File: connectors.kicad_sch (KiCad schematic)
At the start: 4 parts

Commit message: Changes and add component values
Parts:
- gave numbers to parts that had none: 4
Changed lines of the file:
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@@
   (symbol (lib_id "Connector:Conn_01x04_Male") (at 106.68 83.82 0) (unit 1)
     (in_bom yes) (on_board yes)
-    (property "Reference" "J?" (id 0) (at 107.315 76.2 0))
+    (property "Reference" "J1" (id 0) (at 107.315 76.2 0))
     (property "Value" "Conn_01x04_Male" (id 1) (at 107.315 78.74 0))
     (property "Footprint" "" (id 2) (at 106.68 83.82 0)
@@
   (symbol (lib_id "Connector:Conn_01x09_Male") (at 160.02 91.44 0) (unit 1)
     (in_bom yes) (on_board yes)
-    (property "Reference" "J?" (id 0) (at 160.655 76.2 0))
+    (property "Reference" "J3" (id 0) (at 160.655 76.2 0))
     (property "Value" "Conn_01x09_Male" (id 1) (at 160.655 78.74 0))
     (property "Footprint" "" (id 2) (at 160.02 91.44 0)
@@
   (symbol (lib_id "Connector:Conn_01x04_Male") (at 129.54 83.82 0) (unit 1)
     (in_bom yes) (on_board yes)
-    (property "Reference" "J?" (id 0) (at 130.175 76.2 0))
+    (property "Reference" "J2" (id 0) (at 130.175 76.2 0))
     (property "Value" "Conn_01x04_Male" (id 1) (at 130.175 78.74 0))
     (property "Footprint" "" (id 2) (at 129.54 83.82 0)
@@
   (symbol (lib_id "Connector_Generic:Conn_02x03_Odd_Even") (at 187.96 83.82 0) (unit 1)
     (in_bom yes) (on_board yes)
-    (property "Reference" "J?" (id 0) (at 189.23 74.93 0))
+    (property "Reference" "J4" (id 0) (at 189.23 74.93 0))
     (property "Value" "Conn_02x03_Odd_Even" (id 1) (at 189.23 77.47 0))
     (property "Footprint" "" (id 2) (at 187.96 83.82 0)

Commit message: Completed symbol-footprint associations.
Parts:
- J1, J2: footprint (none) -> Connector_PinHeader_2.54mm:PinHeader_1x04_P2.54mm_Vertical
- J3: footprint (none) -> Connector_PinHeader_2.54mm:PinHeader_1x09_P2.54mm_Vertical
- J4: footprint (none) -> Connector_PinHeader_2.54mm:PinHeader_2x03_P2.54mm_Vertical
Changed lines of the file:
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@@
     (property "Reference" "J1" (id 0) (at 107.315 76.2 0))
     (property "Value" "Conn_01x04_Male" (id 1) (at 107.315 78.74 0))
-    (property "Footprint" "" (id 2) (at 106.68 83.82 0)
+    (property "Footprint" "Connector_PinHeader_2.54mm:PinHeader_1x04_P2.54mm_Vertical" (id 2) (at 106.68 83.82 0)
       (effects (font (size 1.27 1.27)) hide)
     )
@@
     (property "Reference" "J3" (id 0) (at 160.655 76.2 0))
     (property "Value" "Conn_01x09_Male" (id 1) (at 160.655 78.74 0))
-    (property "Footprint" "" (id 2) (at 160.02 91.44 0)
+    (property "Footprint" "Connector_PinHeader_2.54mm:PinHeader_1x09_P2.54mm_Vertical" (id 2) (at 160.02 91.44 0)
       (effects (font (size 1.27 1.27)) hide)
     )
@@
     (property "Reference" "J2" (id 0) (at 130.175 76.2 0))
     (property "Value" "Conn_01x04_Male" (id 1) (at 130.175 78.74 0))
-    (property "Footprint" "" (id 2) (at 129.54 83.82 0)
+    (property "Footprint" "Connector_PinHeader_2.54mm:PinHeader_1x04_P2.54mm_Vertical" (id 2) (at 129.54 83.82 0)
       (effects (font (size 1.27 1.27)) hide)
     )
@@
     (property "Reference" "J4" (id 0) (at 189.23 74.93 0))
     (property "Value" "Conn_02x03_Odd_Even" (id 1) (at 189.23 77.47 0))
-    (property "Footprint" "" (id 2) (at 187.96 83.82 0)
+    (property "Footprint" "Connector_PinHeader_2.54mm:PinHeader_2x03_P2.54mm_Vertical" (id 2) (at 187.96 83.82 0)
       (effects (font (size 1.27 1.27)) hide)
     )

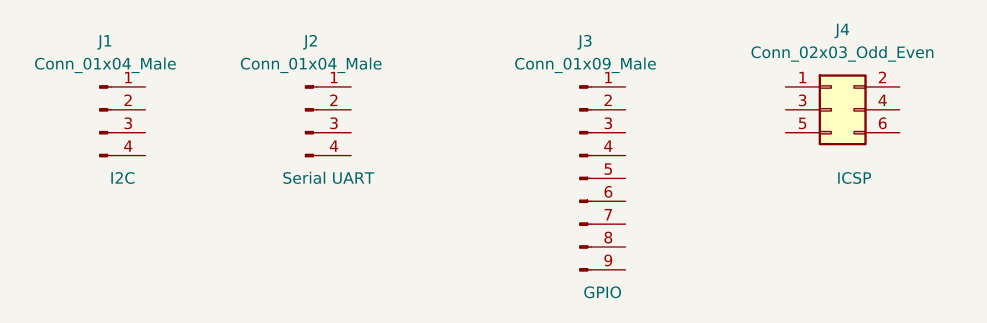
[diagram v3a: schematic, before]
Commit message: Completed wiring
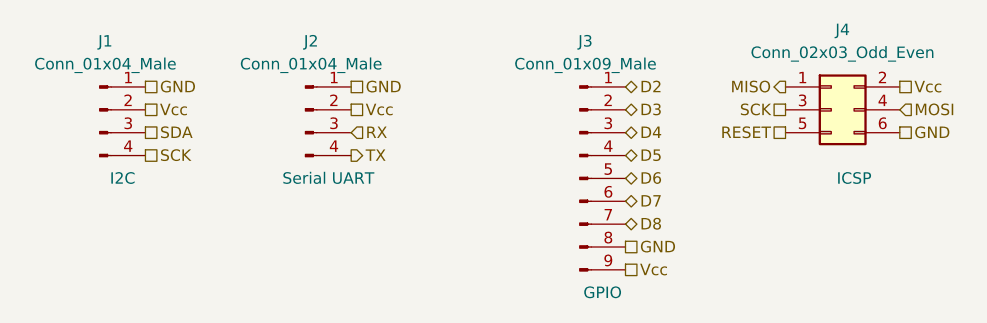
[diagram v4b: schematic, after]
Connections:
- net GND: now reaches J1.1 (Pin_1)
- net GND: now also J2.1 (Pin_1), J3.8 (Pin_8), J4.6 (Pin_6)
- net Vcc: now reaches J1.2 (Pin_2)
- net Vcc: now also J2.2 (Pin_2), J3.9 (Pin_9), J4.2 (Pin_2)
- net SDA: now reaches J1.3 (Pin_3)
- net SCK: now reaches J1.4 (Pin_4)
- net SCK: now also J4.3 (Pin_3)
- net D2: now reaches J3.1 (Pin_1)
- net D3: now reaches J3.2 (Pin_2)
- net D4: now reaches J3.3 (Pin_3)
- net D5: now reaches J3.4 (Pin_4)
- net D6: now reaches J3.5 (Pin_5)
- net D7: now reaches J3.6 (Pin_6)
- net D8: now reaches J3.7 (Pin_7)
- net RX: now reaches J2.3 (Pin_3)
- net TX: now reaches J2.4 (Pin_4)
- net MISO: now reaches J4.1 (Pin_1)
- net MOSI: now reaches J4.4 (Pin_4)
- net RESET: now reaches J4.5 (Pin_5)
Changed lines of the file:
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@@
 (kicad_sch (version 20211123) (generator eeschema)
   (paper "A4")
+  (hierarchical_label "SDA" (shape passive) (at 111.76 86.36 0)
+    (effects (font (size 1.27 1.27)) (justify left))
+  )
+  (hierarchical_label "Vcc" (shape passive) (at 165.1 101.6 0)
+    (effects (font (size 1.27 1.27)) (justify left))
+  )
+  (hierarchical_label "GND" (shape passive) (at 165.1 99.06 0)
+    (effects (font (size 1.27 1.27)) (justify left))
+  )
+  (hierarchical_label "GND" (shape passive) (at 111.76 81.28 0)
+    (effects (font (size 1.27 1.27)) (justify left))
+  )
+  (hierarchical_label "D3" (shape bidirectional) (at 165.1 83.82 0)
+    (effects (font (size 1.27 1.27)) (justify left))
+  )
+  (hierarchical_label "TX" (shape output) (at 134.62 88.9 0)
+    (effects (font (size 1.27 1.27)) (justify left))
+  )
+  (hierarchical_label "GND" (shape passive) (at 134.62 81.28 0)
+    (effects (font (size 1.27 1.27)) (justify left))
+  )
+  (hierarchical_label "D4" (shape bidirectional) (at 165.1 86.36 0)
+    (effects (font (size 1.27 1.27)) (justify left))
+  )
+  (hierarchical_label "MISO" (shape output) (at 182.88 81.28 180)
+    (effects (font (size 1.27 1.27)) (justify right))
+  )
+  (hierarchical_label "Vcc" (shape passive) (at 195.58 81.28 0)
+    (effects (font (size 1.27 1.27)) (justify left))
+  )
+  (hierarchical_label "D5" (shape bidirectional) (at 165.1 88.9 0)
+    (effects (font (size 1.27 1.27)) (justify left))
+  )
+  (hierarchical_label "GND" (shape passive) (at 195.58 86.36 0)
+    (effects (font (size 1.27 1.27)) (justify left))
+  )
+  (hierarchical_label "Vcc" (shape passive) (at 111.76 83.82 0)
+    (effects (font (size 1.27 1.27)) (justify left))
+  )
+  (hierarchical_label "D2" (shape bidirectional) (at 165.1 81.28 0)
+    (effects (font (size 1.27 1.27)) (justify left))
+  )
+  (hierarchical_label "RESET" (shape passive) (at 182.88 86.36 180)
+    (effects (font (size 1.27 1.27)) (justify right))
+  )
+  (hierarchical_label "RX" (shape input) (at 134.62 86.36 0)
+    (effects (font (size 1.27 1.27)) (justify left))
+  )
+  (hierarchical_label "D7" (shape bidirectional) (at 165.1 93.98 0)
+    (effects (font (size 1.27 1.27)) (justify left))
+  )
+  (hierarchical_label "D6" (shape bidirectional) (at 165.1 91.44 0)
+    (effects (font (size 1.27 1.27)) (justify left))
+  )
+  (hierarchical_label "SCK" (shape passive) (at 111.76 88.9 0)
+    (effects (font (size 1.27 1.27)) (justify left))
+  )
+  (hierarchical_label "MOSI" (shape input) (at 195.58 83.82 0)
+    (effects (font (size 1.27 1.27)) (justify left))
+  )
+  (hierarchical_label "Vcc" (shape passive) (at 134.62 83.82 0)
+    (effects (font (size 1.27 1.27)) (justify left))
+  )
+  (hierarchical_label "SCK" (shape passive) (at 182.88 83.82 180)
+    (effects (font (size 1.27 1.27)) (justify right))
+  )
+  (hierarchical_label "D8" (shape bidirectional) (at 165.1 96.52 0)
+    (effects (font (size 1.27 1.27)) (justify left))
+  )
   (symbol (lib_id "Connector:Conn_01x04_Male") (at 106.68 83.82 0) (unit 1)
     (in_bom yes) (on_board yes)
